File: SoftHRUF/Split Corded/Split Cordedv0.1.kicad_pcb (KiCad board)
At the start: 2 copper layers, 231.2 x 70.7 mm, 98 parts, among them CON1 AVR-ISP-6, P1 USB_B, P2 10p10c_LEFT, P3 10p10c_RIGHT, SW1 SW_PUSH, SW10 SW_PUSH, SW11 SW_PUSH, SW12 SW_PUSH, SW13 SW_PUSH, SW14 SW_PUSH, SW15 SW_PUSH, SW16 SW_PUSH, SW17 SW_PUSH, SW18 SW_PUSH, SW19 SW_PUSH, SW2 SW_PUSH, SW20 SW_PUSH, SW21 SW_PUSH, SW22 SW_PUSH, SW23 SW_PUSH, SW24 SW_PUSH, SW25 SW_PUSH, SW26 SW_PUSH, SW27 SW_PUSH, SW28 SW_PUSH, SW29 SW_PUSH, SW3 SW_PUSH, SW30 SW_PUSH, SW31 SW_PUSH, SW32 SW_PUSH, SW33 SW_PUSH, SW34 SW_PUSH, SW35 SW_PUSH, SW36 SW_PUSH, SW37 SW_PUSH, SW38 SW_PUSH, SW39 SW_PUSH, SW4 SW_PUSH, SW40 SW_PUSH, SW41 Switch_DPST, SW5 SW_PUSH, SW6 SW_PUSH, SW7 SW_PUSH, SW8 SW_PUSH, SW9 SW_PUSH, U1 IP4234CZ6, U2 ATmega32U4-AU, Y1 Crystal_Small

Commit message: All connections checked, all ground and VCC connections specifically. Awaiting final tests in the lab on current prototype before finalizing.
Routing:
- net (no net): track 841.6 -> 850.4 mm, vias 1 -> 5
- net +5V: track 51.9 -> 57.8 mm
- net GND: track 55.0 -> 53.6 mm, vias 12 -> 11
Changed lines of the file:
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@@
-(kicad_pcb (version 4) (host pcbnew 4.0.1-stable)
+(kicad_pcb (version 4) (host pcbnew 4.0.5)
   (general
     (links 177)
-    (no_connects 0)
-    (area -0.075001 -5.775001 231.275001 65.075001)
+    (no_connects 1)
+    (area -0.45 -8.785 474.675002 229.425002)
     (thickness 1.6)
     (drawings 17)
-    (tracks 750)
+    (tracks 758)
     (zones 0)
     (modules 98)
@@
     (pad_to_mask_clearance 0.2)
     (aux_axis_origin 0 0)
-    (visible_elements FFFFFFFF)
+    (visible_elements FFFFEFFF)
     (pcbplotparams
       (layerselection 0x3f0ff_80000001)
@@
     (add_net "Net-(R3-Pad1)")
   )
+  (module Capacitors_SMD:C_0603 (layer B.Cu)
+    (at 60.7 8.8)
+    (descr "Capacitor SMD 0603, reflow soldering, AVX (see smccp.pdf)")
+    (tags "capacitor 0603")
+    (attr smd)
+    (fp_text reference C2 (at 0 1.9) (layer B.SilkS)
+      (effects (font (size 1 1) (thickness 0.15)) (justify mirror))
+    )
+    (fp_text value 10uF (at 0 -1.9) (layer B.Fab)
+      (effects (font (size 1 1) (thickness 0.15)) (justify mirror))
+    )
+    (fp_line (start -1.45 0.75) (end 1.45 0.75) (layer B.CrtYd) (width 0.05))
+    (fp_line (start -1.45 -0.75) (end 1.45 -0.75) (layer B.CrtYd) (width 0.05))
+    (fp_line (start -1.45 0.75) (end -1.45 -0.75) (layer B.CrtYd) (width 0.05))
+    (fp_line (start 1.45 0.75) (end 1.45 -0.75) (layer B.CrtYd) (width 0.05))
+    (fp_line (start -0.35 0.6) (end 0.35 0.6) (layer B.SilkS) (width 0.15))
+    (fp_line (start 0.35 -0.6) (end -0.35 -0.6) (layer B.SilkS) (width 0.15))
+    (pad 1 smd rect (at -0.75 0) (size 0.8 0.75) (layers B.Cu B.Paste B.Mask)
+      (net 2 +5V))
+    (pad 2 smd rect (at 0.75 0) (size 0.8 0.75) (layers B.Cu B.Paste B.Mask)
+      (net 1 GND))
+    (model Capacitors_SMD.3dshapes/C_0603.wrl
+      (at (xyz 0 0 0))
+      (scale (xyz 1 1 1))
+      (rotate (xyz 0 0 0))
+    )
+  )
   (module Buttons_Switches_ThroughHole:SW_Matias_Quiet_With_Mounting_Hole_Frame (layer F.Cu)
     (at 74 15.8)
@@
   )
   (module Capacitors_SMD:C_0603 (layer B.Cu)
-    (at 60.7 8.8)
-    (descr "Capacitor SMD 0603, reflow soldering, AVX (see smccp.pdf)")
-    (tags "capacitor 0603")
-    (attr smd)
-    (fp_text reference C2 (at 0 1.9) (layer B.SilkS)
-      (effects (font (size 1 1) (thickness 0.15)) (justify mirror))
-    )
-    (fp_text value 10uF (at 0 -1.9) (layer B.Fab)
-      (effects (font (size 1 1) (thickness 0.15)) (justify mirror))
-    )
-    (fp_line (start -1.45 0.75) (end 1.45 0.75) (layer B.CrtYd) (width 0.05))
-    (fp_line (start -1.45 -0.75) (end 1.45 -0.75) (layer B.CrtYd) (width 0.05))
-    (fp_line (start -1.45 0.75) (end -1.45 -0.75) (layer B.CrtYd) (width 0.05))
-    (fp_line (start 1.45 0.75) (end 1.45 -0.75) (layer B.CrtYd) (width 0.05))
-    (fp_line (start -0.35 0.6) (end 0.35 0.6) (layer B.SilkS) (width 0.15))
-    (fp_line (start 0.35 -0.6) (end -0.35 -0.6) (layer B.SilkS) (width 0.15))
-    (pad 1 smd rect (at -0.75 0) (size 0.8 0.75) (layers B.Cu B.Paste B.Mask)
-      (net 2 +5V))
-    (pad 2 smd rect (at 0.75 0) (size 0.8 0.75) (layers B.Cu B.Paste B.Mask)
-      (net 1 GND))
-    (model Capacitors_SMD.3dshapes/C_0603.wrl
-      (at (xyz 0 0 0))
-      (scale (xyz 1 1 1))
-      (rotate (xyz 0 0 0))
-    )
-  )
-  (module Capacitors_SMD:C_0603 (layer B.Cu)
     (at 65.84 4.85)
     (descr "Capacitor SMD 0603, reflow soldering, AVX (see smccp.pdf)")
@@
   (gr_line (start 0 -2) (end 0 45) (layer Edge.Cuts) (width 0.15))
   (gr_line (start 108 -2) (end 231.2 -2) (layer Edge.Cuts) (width 0.15))
+  (segment (start 57.16 2.14) (end 54.08 5.22) (width 0.25) (layer F.Cu) (net 0))
+  (segment (start 54.08 5.22) (end 51.9 5.22) (width 0.25) (layer F.Cu) (net 0))
+  (via (at 51.9 5.22) (size 0.6) (drill 0.4) (layers F.Cu B.Cu) (net 0))
+  (segment (start 57.14 2.12) (end 57.16 2.14) (width 0.25) (layer B.Cu) (net 0))
+  (via (at 57.16 2.14) (size 0.6) (drill 0.4) (layers F.Cu B.Cu) (net 0))
+  (segment (start 8.43 26.14) (end 8.43 25.9) (width 0.25) (layer F.Cu) (net 0))
+  (segment (start 8.43 25.9) (end 7.02 24.49) (width 0.25) (layer F.Cu) (net 0))
+  (via (at 7.02 24.49) (size 0.6) (drill 0.4) (layers F.Cu B.Cu) (net 0))
+  (segment (start 8.43 26.17) (end 8.43 26.14) (width 0.25) (layer B.Cu) (net 0))
+  (via (at 8.43 26.14) (size 0.6) (drill 0.4) (layers F.Cu B.Cu) (net 0))
   (segment (start 465.2 182.25006) (end 446.6 182.25006) (width 0.25) (layer B.Cu) (net 0))
   (segment (start 428.2 182.15006) (end 446.5 182.15006) (width 0.25) (layer B.Cu) (net 0))
@@
   (segment (start 474.35 203.8) (end 474.35 201.67868) (width 0.25) (layer F.Cu) (net 0))
   (segment (start 474.35 201.67868) (end 474.35 188) (width 0.25) (layer F.Cu) (net 0))
+  (segment (start 67.026004 11.266727) (end 66.70779 11.266727) (width 0.25) (layer B.Cu) (net 1))
+  (segment (start 66.70779 11.266727) (end 66.10675 11.867767) (width 0.25) (layer B.Cu) (net 1))
+  (segment (start 67.302732 10.989999) (end 67.026004 11.266727) (width 0.25) (layer B.Cu) (net 1))
   (segment (start 68.28 10.69) (end 67.980001 10.989999) (width 0.25) (layer B.Cu) (net 1))
   (segment (start 67.980001 10.989999) (end 67.302732 10.989999) (width 0.25) (layer B.Cu) (net 1))
-  (segment (start 67.302732 10.989999) (end 67.026004 11.266727) (width 0.25) (layer B.Cu) (net 1))
   (segment (start 67.66 10.008293) (end 67.66 10.07) (width 0.25) (layer F.Cu) (net 1))
   (segment (start 67.66 10.07) (end 68.28 10.69) (width 0.25) (layer F.Cu) (net 1))
@@
   (segment (start 71.233273 15.79221) (end 71.233273 15.473996) (width 0.25) (layer B.Cu) (net 1))
   (segment (start 71.233273 15.473996) (end 67.026004 11.266727) (width 0.25) (layer B.Cu) (net 1))
-  (segment (start 66.70779 11.266727) (end 66.10675 11.867767) (width 0.25) (layer B.Cu) (net 1))
-  (segment (start 67.026004 11.266727) (end 66.70779 11.266727) (width 0.25) (layer B.Cu) (net 1))
   (segment (start 66.780578 5.859422) (end 67.028051 5.859422) (width 0.25) (layer B.Cu) (net 1))
   (segment (start 67.028051 5.859422) (end 67.803806 6.635177) (width 0.25) (layer B.Cu) (net 1))
@@
   (via (at 81.37 11.3) (size 0.6) (drill 0.4) (layers F.Cu B.Cu) (net 1))
   (segment (start 70.632233 16.39325) (end 70.632233 16.367767) (width 0.25) (layer B.Cu) (net 1))
-  (segment (start 66.10675 11.867767) (end 66.052233 11.867767) (width 0.25) (layer B.Cu) (net 1))
-  (segment (start 66.052233 11.867767) (end 65.08 12.84) (width 0.25) (layer B.Cu) (net 1))
-  (via (at 65.08 12.84) (size 0.6) (drill 0.4) (layers F.Cu B.Cu) (net 1))
   (segment (start 63.5 4.85) (end 63.5 4.57) (width 0.25) (layer B.Cu) (net 1))
   (segment (start 63.5 4.57) (end 64.3 3.77) (width 0.25) (layer B.Cu) (net 1))
@@
   (segment (start 55.26 -0.23) (end 55.57 0.08) (width 0.25) (layer B.Cu) (net 1))
   (via (at 55.57 0.08) (size 0.6) (drill 0.4) (layers F.Cu B.Cu) (net 1))
+  (segment (start 74.733452 4.372435) (end 73.001041 6.104846) (width 0.25) (layer B.Cu) (net 2))
+  (segment (start 73.001041 6.104846) (end 69.536217 6.104846) (width 0.25) (layer B.Cu) (net 2))
+  (segment (start 69.536217 6.104846) (end 68.935177 5.503806) (width 0.25) (layer B.Cu) (net 2))
   (segment (start 71.197918 16.958936) (end 71.197918 16.676109) (width 0.25) (layer B.Cu) (net 2))
   (segment (start 71.683282 16.190745) (end 71.683282 13.16828) (width 0.25) (layer B.Cu) (net 2))
@@
   (segment (start 67.396727 8.893273) (end 69.536217 6.753783) (width 0.25) (layer B.Cu) (net 2))
   (segment (start 69.536217 6.753783) (end 69.536217 6.104846) (width 0.25) (layer B.Cu) (net 2))
-  (segment (start 69.536217 6.104846) (end 68.935177 5.503806) (width 0.25) (layer B.Cu) (net 2))
   (segment (start 67.396727 8.933273) (end 67.396727 8.893273) (width 0.25) (layer B.Cu) (net 2))
   (segment (start 77.41 10.13) (end 77.709999 9.830001) (width 0.25) (layer F.Cu) (net 2))
@@
   (segment (start 47.25 17.7) (end 49.32468 15.62532) (width 0.25) (layer B.Cu) (net 53))
   (segment (start 49.32468 15.62532) (end 66.591853 15.62532) (width 0.25) (layer B.Cu) (net 53))
-  (segment (start 68.086664 14.130509) (end 68.369491 14.130509) (width 0.25) (layer B.Cu) (net 53))
   (segment (start 66.591853 15.62532) (end 68.086664 14.130509) (width 0.25) (layer B.Cu) (net 53))
   (segment (start 47.25 17.7) (end 47.25 19.82132) (width 0.25) (layer F.Cu) (net 53))

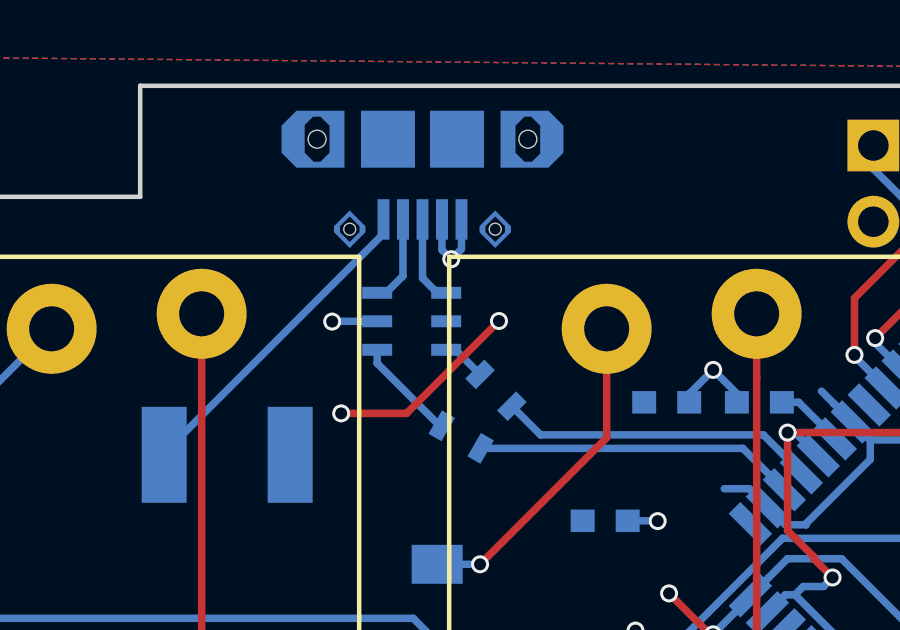
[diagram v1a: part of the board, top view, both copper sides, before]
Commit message: In the middle of making last few changes. Last thing I need to do is fiddle with the USB connector, since the first one showed signs of weakness.
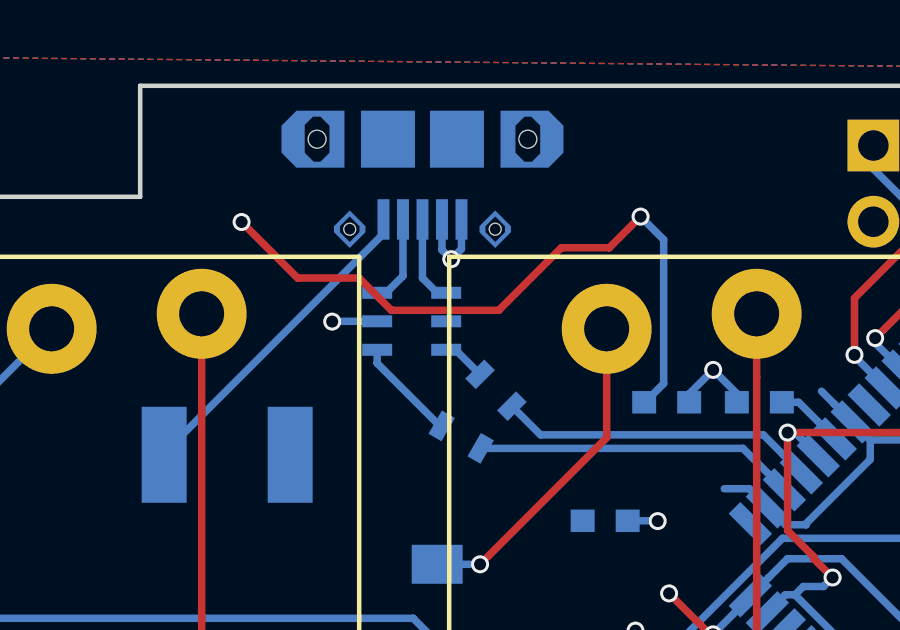
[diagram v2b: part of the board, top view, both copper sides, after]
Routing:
- net +5V: track 57.8 -> 80.4 mm, vias 6 -> 8
- net (no net): track 850.4 -> 843.9 mm, vias 5 -> 3
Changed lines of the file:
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@@
   (general
     (links 177)
-    (no_connects 1)
+    (no_connects 0)
     (area -0.45 -8.785 474.675002 229.425002)
     (thickness 1.6)
     (drawings 17)
-    (tracks 758)
+    (tracks 766)
     (zones 0)
     (modules 98)
@@
   (page A4)
   (layers
-    (0 F.Cu signal)
+    (0 F.Cu signal hide)
     (31 B.Cu signal)
     (32 B.Adhes user)
@@
   (gr_line (start 0 -2) (end 0 45) (layer Edge.Cuts) (width 0.15))
   (gr_line (start 108 -2) (end 231.2 -2) (layer Edge.Cuts) (width 0.15))
-  (segment (start 57.16 2.14) (end 54.08 5.22) (width 0.25) (layer F.Cu) (net 0))
-  (segment (start 54.08 5.22) (end 51.9 5.22) (width 0.25) (layer F.Cu) (net 0))
-  (via (at 51.9 5.22) (size 0.6) (drill 0.4) (layers F.Cu B.Cu) (net 0))
-  (segment (start 57.14 2.12) (end 57.16 2.14) (width 0.25) (layer B.Cu) (net 0))
-  (via (at 57.16 2.14) (size 0.6) (drill 0.4) (layers F.Cu B.Cu) (net 0))
   (segment (start 8.43 26.14) (end 8.43 25.9) (width 0.25) (layer F.Cu) (net 0))
   (segment (start 8.43 25.9) (end 7.02 24.49) (width 0.25) (layer F.Cu) (net 0))
@@
   (segment (start 55.26 -0.23) (end 55.57 0.08) (width 0.25) (layer B.Cu) (net 1))
   (via (at 55.57 0.08) (size 0.6) (drill 0.4) (layers F.Cu B.Cu) (net 1))
+  (segment (start 52.5 0.71) (end 50.45 0.71) (width 0.25) (layer F.Cu) (net 2))
+  (segment (start 50.45 0.71) (end 48.58 -1.16) (width 0.25) (layer F.Cu) (net 2))
+  (via (at 48.58 -1.16) (size 0.6) (drill 0.4) (layers F.Cu B.Cu) (net 2))
+  (segment (start 53.57 1.78) (end 52.5 0.71) (width 0.25) (layer F.Cu) (net 2))
+  (segment (start 57.16 1.78) (end 53.57 1.78) (width 0.25) (layer F.Cu) (net 2))
+  (segment (start 59.24 -0.3) (end 57.16 1.78) (width 0.25) (layer F.Cu) (net 2))
+  (segment (start 60.84 -0.3) (end 59.24 -0.3) (width 0.25) (layer F.Cu) (net 2))
+  (segment (start 61.88 -1.34) (end 60.84 -0.3) (width 0.25) (layer F.Cu) (net 2))
+  (segment (start 62 4.85) (end 62.025 4.85) (width 0.25) (layer B.Cu) (net 2))
+  (segment (start 62.025 4.85) (end 62.65 4.225) (width 0.25) (layer B.Cu) (net 2))
+  (segment (start 62.65 4.225) (end 62.65 -0.57) (width 0.25) (layer B.Cu) (net 2))
+  (segment (start 62.65 -0.57) (end 61.88 -1.34) (width 0.25) (layer B.Cu) (net 2))
+  (via (at 61.88 -1.34) (size 0.6) (drill 0.4) (layers F.Cu B.Cu) (net 2))
   (segment (start 74.733452 4.372435) (end 73.001041 6.104846) (width 0.25) (layer B.Cu) (net 2))
   (segment (start 73.001041 6.104846) (end 69.536217 6.104846) (width 0.25) (layer B.Cu) (net 2))
